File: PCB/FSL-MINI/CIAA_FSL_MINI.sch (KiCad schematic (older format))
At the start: 13 parts, among them P103 CONN_01X05

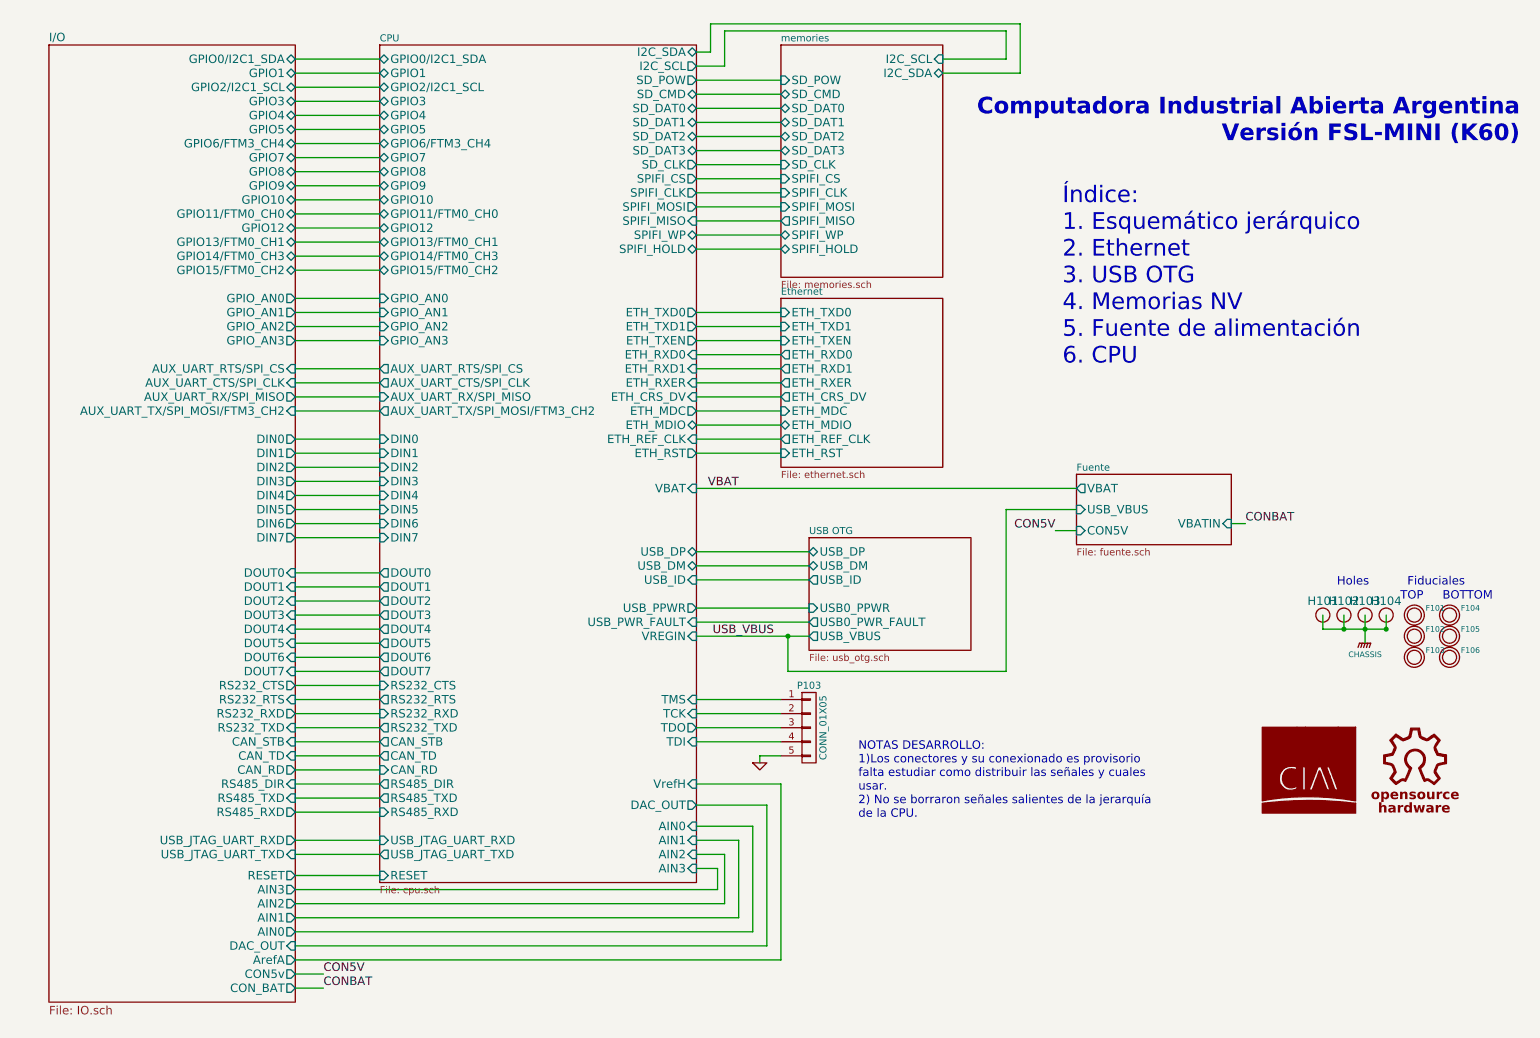
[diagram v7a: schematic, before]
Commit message: Swap ethernet schematic sheet for CIAA NXP ethernet sheet. Preliminary schematic finished. Add notas.txt file.
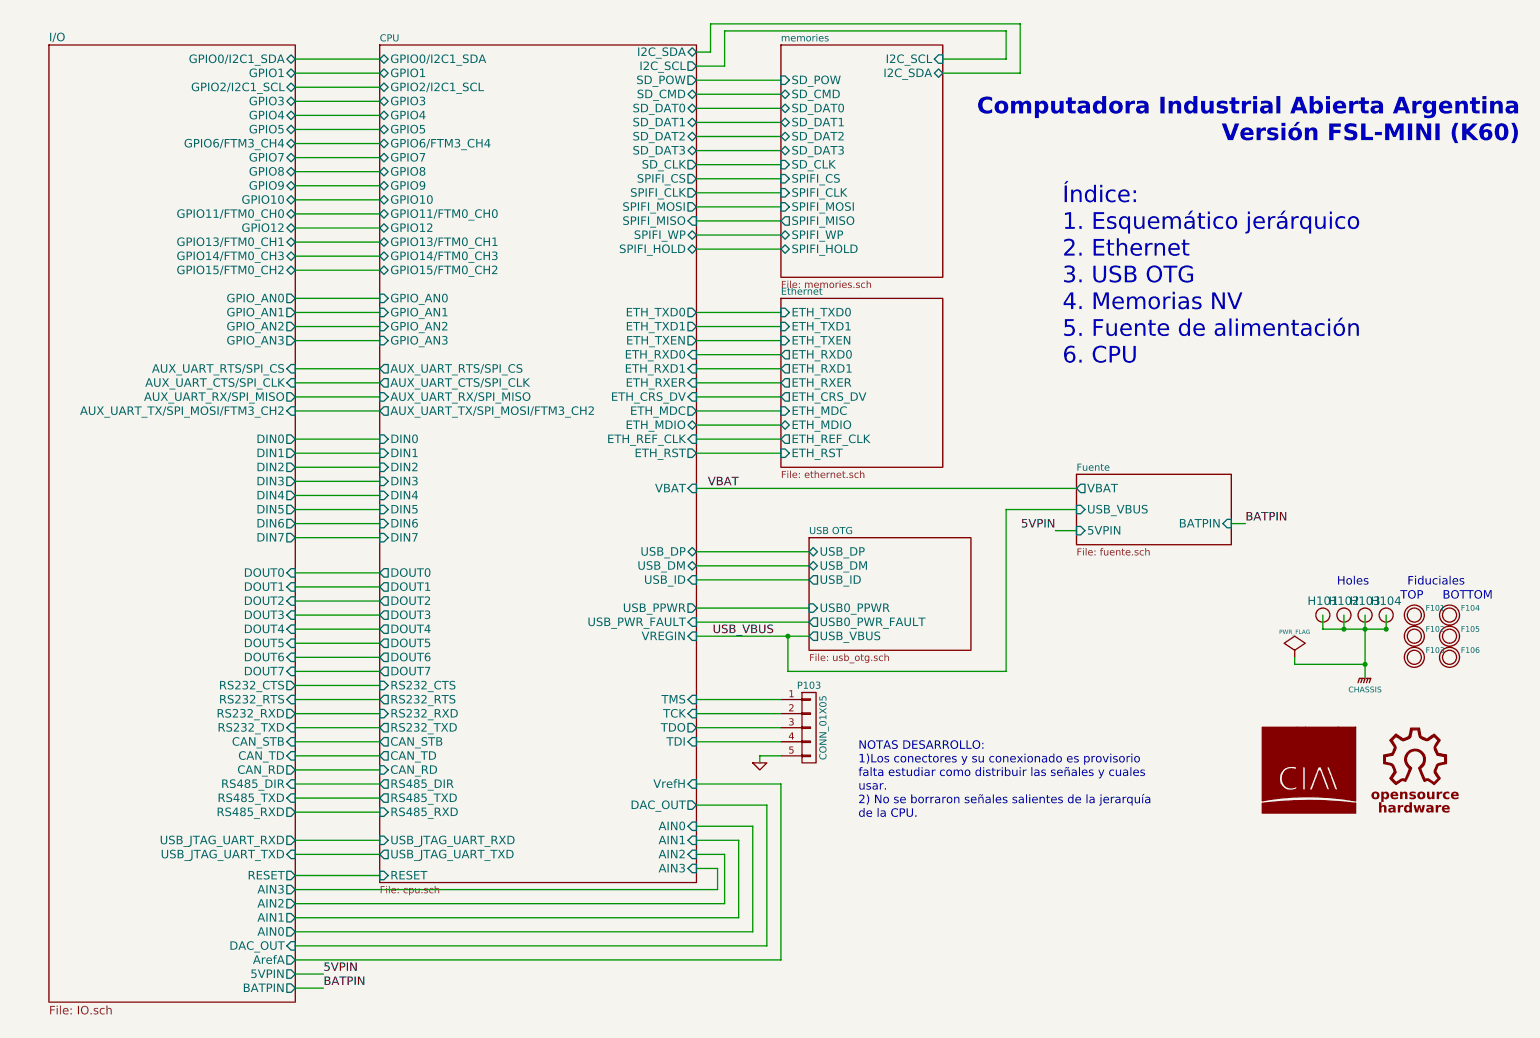
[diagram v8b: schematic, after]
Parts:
- F101, F102, F103, F104, F105, F106: footprint footprints:Fiducial_1mm -> FSL-MINI:Fiducial_1mm
- G101: footprint footprints:LOGO-CIAA -> FSL-MINI:LOGO-CIAA
- G102: footprint footprints:OSHWA -> FSL-MINI:OSHWA
- H101, H102, H103, H104: footprint footprints:PCB_HOLE -> FSL-MINI:PCB_HOLE
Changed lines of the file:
@@
 EESchema Schematic File Version 2
-LIBS:TXB0108
 LIBS:CIAAK60LIB
 LIBS:conn
@@
 F2 "USB_VBUS" I L 7950 4050 60
 F3 "VBAT" O L 7950 3900 60
-F4 "VBATIN" I R 9050 4150 60
-F5 "CON5V" I L 7950 4200 60
+F4 "BATPIN" I R 9050 4150 60
+F5 "5VPIN" I L 7950 4200 60
 $EndSheet
 Text Notes 7850 3600 0    118  ~ 0
@@
 F 0 "F101" H 10430 4850 40  0000 L CNN
 F 1 "FIDUCIAL" H 10350 4700 30  0001 C CNN
-F 2 "footprints:Fiducial_1mm" H 10350 4850 60  0001 C CNN
+F 2 "FSL-MINI:Fiducial_1mm" H 10350 4850 60  0001 C CNN
 F 3 "~" H 10350 4850 60  0001 C CNN
 F 4 "FIDUCIAL" H 10400 4600 60  0001 C CNN "Descripcion"
@@
 F 0 "H101" H 9700 4900 60  0000 C CNN
 F 1 "PCB_HOLE" H 9750 4700 60  0001 C CNN
-F 2 "footprints:PCB_HOLE" H 9550 4850 60  0001 C CNN
+F 2 "FSL-MINI:PCB_HOLE" H 9550 4850 60  0001 C CNN
 F 3 "~" H 9650 4950 60  0001 C CNN
 F 4 "PCB HOLE" H 9750 5050 60  0001 C CNN "Descripcion"
@@
 F 0 "F102" H 10430 5000 40  0000 L CNN
 F 1 "FIDUCIAL" H 10350 4850 30  0001 C CNN
-F 2 "footprints:Fiducial_1mm" H 10350 5000 60  0001 C CNN
+F 2 "FSL-MINI:Fiducial_1mm" H 10350 5000 60  0001 C CNN
 F 3 "~" H 10350 5000 60  0001 C CNN
 F 4 "FIDUCIAL" H 10400 4750 60  0001 C CNN "Descripcion"
@@
 F 0 "F103" H 10430 5150 40  0000 L CNN
 F 1 "FIDUCIAL" H 10350 5000 30  0001 C CNN
-F 2 "footprints:Fiducial_1mm" H 10350 5150 60  0001 C CNN
+F 2 "FSL-MINI:Fiducial_1mm" H 10350 5150 60  0001 C CNN
 F 3 "~" H 10350 5150 60  0001 C CNN
 F 4 "FIDUCIAL" H 10400 4900 60  0001 C CNN "Descripcion"
@@
 F 0 "F104" H 10680 4850 40  0000 L CNN
 F 1 "FIDUCIAL" H 10600 4700 30  0001 C CNN
-F 2 "footprints:Fiducial_1mm" H 10600 4850 60  0001 C CNN
+F 2 "FSL-MINI:Fiducial_1mm" H 10600 4850 60  0001 C CNN
 F 3 "~" H 10600 4850 60  0001 C CNN
 F 4 "FIDUCIAL" H 10650 4600 60  0001 C CNN "Descripcion"
@@
 F 0 "F105" H 10680 5000 40  0000 L CNN
 F 1 "FIDUCIAL" H 10600 4850 30  0001 C CNN
-F 2 "footprints:Fiducial_1mm" H 10600 5000 60  0001 C CNN
+F 2 "FSL-MINI:Fiducial_1mm" H 10600 5000 60  0001 C CNN
 F 3 "~" H 10600 5000 60  0001 C CNN
 F 4 "FIDUCIAL" H 10650 4750 60  0001 C CNN "Descripcion"
@@
 F 0 "F106" H 10680 5150 40  0000 L CNN
 F 1 "FIDUCIAL" H 10600 5000 30  0001 C CNN
-F 2 "footprints:Fiducial_1mm" H 10600 5150 60  0001 C CNN
+F 2 "FSL-MINI:Fiducial_1mm" H 10600 5150 60  0001 C CNN
 F 3 "~" H 10600 5150 60  0001 C CNN
 F 4 "FIDUCIAL" H 10650 4900 60  0001 C CNN "Descripcion"
@@
 F 0 "H102" H 9850 4900 60  0000 C CNN
 F 1 "PCB_HOLE" H 9900 4700 60  0001 C CNN
-F 2 "footprints:PCB_HOLE" H 9700 4850 60  0001 C CNN
+F 2 "FSL-MINI:PCB_HOLE" H 9700 4850 60  0001 C CNN
 F 3 "~" H 9800 4950 60  0001 C CNN
 F 4 "PCB HOLE" H 9900 5050 60  0001 C CNN "Descripcion"
@@
 F 0 "H103" H 10000 4900 60  0000 C CNN
 F 1 "PCB_HOLE" H 10050 4700 60  0001 C CNN
-F 2 "footprints:PCB_HOLE" H 9850 4850 60  0001 C CNN
+F 2 "FSL-MINI:PCB_HOLE" H 9850 4850 60  0001 C CNN
 F 3 "~" H 9950 4950 60  0001 C CNN
 F 4 "PCB HOLE" H 10050 5050 60  0001 C CNN "Descripcion"
@@
 F 0 "H104" H 10150 4900 60  0000 C CNN
 F 1 "PCB_HOLE" H 10200 4700 60  0001 C CNN
-F 2 "footprints:PCB_HOLE" H 10000 4850 60  0001 C CNN
+F 2 "FSL-MINI:PCB_HOLE" H 10000 4850 60  0001 C CNN
 F 3 "~" H 10100 4950 60  0001 C CNN
 F 4 "PCB HOLE" H 10200 5050 60  0001 C CNN "Descripcion"
@@
 F 0 "G102" H 10320 6300 60  0001 C CNN
 F 1 "OSHWA" H 10350 6203 60  0001 C CNN
-F 2 "footprints:OSHWA" H 10350 5900 60  0001 C CNN
+F 2 "FSL-MINI:OSHWA" H 10350 5900 60  0001 C CNN
 F 3 "~" H 10350 5900 60  0000 C CNN
 F 4 "LOGO DE OPEN SOURCE HARDWARE" H 10350 5900 60  0001 C CNN "Descripcion"
@@
 L CHASSIS #PWR01
 U 1 1 53A211E1
-P 10000 5000
-F 0 "#PWR01" H 10000 5050 40  0001 C CNN
-F 1 "CHASSIS" H 10000 4920 40  0000 C CNN
-F 2 "" H 10000 5000 60  0000 C CNN
-F 3 "" H 10000 5000 60  0000 C CNN
-	1    10000 5000
+P 10000 5250
+F 0 "#PWR01" H 10000 5300 40  0001 C CNN
+F 1 "CHASSIS" H 10000 5170 40  0000 C CNN
+F 2 "" H 10000 5250 60  0000 C CNN
+F 3 "" H 10000 5250 60  0000 C CNN
+	1    10000 5250
 	1    0    0    -1
 $EndComp
@@
 F 0 "G101" H 9600 5327 60  0001 C CNN
 F 1 "LOGO_CIAA" H 9600 6473 60  0001 C CNN
-F 2 "footprints:LOGO-CIAA" H 9600 5900 60  0001 C CNN
+F 2 "FSL-MINI:LOGO-CIAA" H 9600 5900 60  0001 C CNN
 F 3 "~" H 9600 5900 60  0000 C CNN
 F 4 "LOGO CIAA" H 9600 5900 60  0001 C CNN "Descripcion"
@@
 $EndComp
 Text Label 9150 4150 0    60   ~ 0
-CONBAT
+BATPIN
 $Sheet
 S 3000 750  2250 5950
@@
 $EndSheet
 Text Label 7800 4200 2    60   ~ 0
-CON5V
+5VPIN
 $Comp
 L CONN_01X05 P103
@@
 	5250 1600 5850 1600
 Wire Wire Line
-	10000 4800 10000 5000
+	10000 4800 10000 5250
 Wire Wire Line
 	9850 4800 9850 4900
@@
 F59 "GPIO15/FTM0_CH2" B R 2400 2350 60
 F60 "AUX_UART_TX/SPI_MOSI/FTM3_CH2" I R 2400 3350 60
-F61 "CON5v" O R 2400 7350 60
-F62 "CON_BAT" O R 2400 7450 60
+F61 "5VPIN" O R 2400 7350 60
+F62 "BATPIN" O R 2400 7450 60
 $EndSheet
 Wire Wire Line
@@
 	2400 6650 3000 6650
 Text Label 2600 7350 0    60   ~ 0
-CON5V
+5VPIN
 Wire Wire Line
 	2400 7350 2600 7350
 Text Label 2600 7450 0    60   ~ 0
-CONBAT
+BATPIN
 Wire Wire Line
 	2600 7450 2400 7450
+$Comp
+L PWR_FLAG #FLG03
+U 1 1 5775BDC5
+P 9500 5100
+F 0 "#FLG03" H 9500 5195 30  0001 C CNN
+F 1 "PWR_FLAG" H 9500 5280 30  0000 C CNN
+F 2 "" H 9500 5100 60  0000 C CNN
+F 3 "" H 9500 5100 60  0000 C CNN
+	1    9500 5100
+	1    0    0    -1
+$EndComp
+Wire Wire Line
+	9500 5100 9500 5150
+Wire Wire Line
+	9500 5150 10000 5150
+Connection ~ 10000 5150
 $EndSCHEMATC
